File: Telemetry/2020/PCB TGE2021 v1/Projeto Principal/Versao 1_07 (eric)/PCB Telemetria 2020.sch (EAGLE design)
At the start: 58 parts, among them IC1 INA240A1DR, IC2 MCP3221A6T-E_OTVAO, IC3 AZ1117IH-3.3TRG1, IC4 ACS758LCB-050B-PFF-T, IC5 ADS1115IDGSR, IC6 ACS712-030B3, IC7 THVD2410DR, IC8 TMP235AEDCKRQ1, J1 172042-0406, J2 43045-0412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

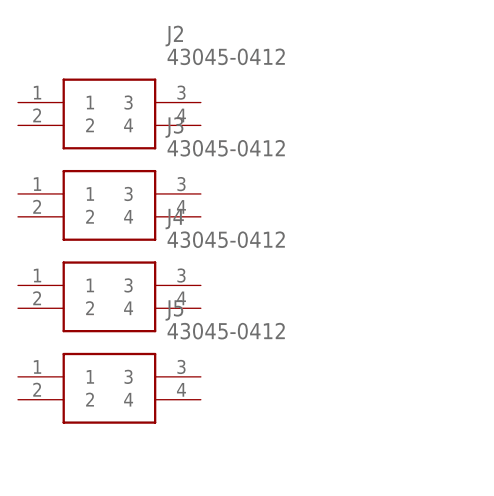
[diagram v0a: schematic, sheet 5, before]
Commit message: Final v1.07
Final version with extra connectors and temperature sensor wired properly
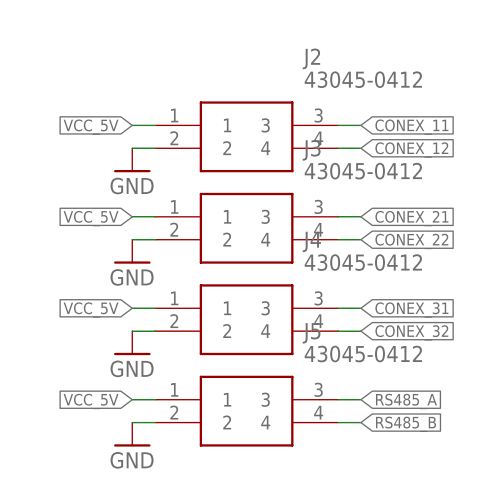
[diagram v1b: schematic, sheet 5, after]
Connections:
- removed net N$14: D2.1, IC7.B, R14.2, RJ11_1.4, RJ11_2.4
- removed net N$9: D1.1, IC7.A, R14.1, RJ11_1.2, RJ11_2.2
- new net RS485_A: D1.1, IC7.A, J5.3, R14.1, RJ11_1.2, RJ11_2.2
- new net RS485_B: D2.1, IC7.B, J5.4, R14.2, RJ11_1.4, RJ11_2.4
- net CONEX_11: now also J2.3
- net CONEX_12: now also J2.4
- net CONEX_21: now also J3.3
- net CONEX_22: now also J3.4
- net CONEX_31: now also J4.3
- net CONEX_32: now also J4.4
- net GND: now also J2.2, J3.2, J4.2, J5.2
- net VCC_5V: now also J2.1, J3.1, J4.1, J5.1
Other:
- moved on the sheet: J2, J3, J4, J5
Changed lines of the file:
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@@
 <?xml version="1.0" encoding="utf-8"?>
 <!DOCTYPE eagle SYSTEM "eagle.dtd">
-<eagle version="9.5.2">
+<eagle version="9.6.2">
 <drawing>
 <settings>
@@
 <part name="RJ11_2" library="Painel-Facilidades" deviceset="TFC44" device=""/>
 <part name="SUPPLY7" library="supply2" library_urn="urn:adsk.eagle:library:372" deviceset="GND" device=""/>
+<part name="GND20" library="supply1" library_urn="urn:adsk.eagle:library:371" deviceset="GND" device=""/>
+<part name="GND21" library="supply1" library_urn="urn:adsk.eagle:library:371" deviceset="GND" device=""/>
+<part name="GND22" library="supply1" library_urn="urn:adsk.eagle:library:371" deviceset="GND" device=""/>
+<part name="GND23" library="supply1" library_urn="urn:adsk.eagle:library:371" deviceset="GND" device=""/>
 </parts>
 <sheets>
@@
 </segment>
 </net>
-<net name="N$9" class="0">
+<net name="RS485_A" class="0">
 <segment>
 <pinref part="D1" gate="G$1" pin="1"/>
@@
 </segment>
 </net>
-<net name="N$14" class="0">
+<net name="RS485_B" class="0">
 <segment>
 <pinref part="IC7" gate="G$1" pin="B"/>
@@
 <attribute name="SHEET" x="357.505" y="5.08" size="2.54" layer="94"/>
 </instance>
-<instance part="J2" gate="G$1" x="15.24" y="246.38" smashed="yes">
-<attribute name="NAME" x="31.75" y="254" size="1.778" layer="95" align="center-left"/>
-<attribute name="VALUE" x="31.75" y="251.46" size="1.778" layer="96" align="center-left"/>
-</instance>
-<instance part="J3" gate="G$1" x="15.24" y="236.22" smashed="yes">
-<attribute name="NAME" x="31.75" y="243.84" size="1.778" layer="95" align="center-left"/>
-<attribute name="VALUE" x="31.75" y="241.3" size="1.778" layer="96" align="center-left"/>
-</instance>
-<instance part="J4" gate="G$1" x="15.24" y="226.06" smashed="yes">
-<attribute name="NAME" x="31.75" y="233.68" size="1.778" layer="95" align="center-left"/>
-<attribute name="VALUE" x="31.75" y="231.14" size="1.778" layer="96" align="center-left"/>
-</instance>
-<instance part="J5" gate="G$1" x="15.24" y="215.9" smashed="yes">
-<attribute name="NAME" x="31.75" y="223.52" size="1.778" layer="95" align="center-left"/>
-<attribute name="VALUE" x="31.75" y="220.98" size="1.778" layer="96" align="center-left"/>
+<instance part="J2" gate="G$1" x="30.48" y="243.84" smashed="yes">
+<attribute name="NAME" x="46.99" y="251.46" size="1.778" layer="95" align="center-left"/>
+<attribute name="VALUE" x="46.99" y="248.92" size="1.778" layer="96" align="center-left"/>
+</instance>
+<instance part="J3" gate="G$1" x="30.48" y="233.68" smashed="yes">
+<attribute name="NAME" x="46.99" y="241.3" size="1.778" layer="95" align="center-left"/>
+<attribute name="VALUE" x="46.99" y="238.76" size="1.778" layer="96" align="center-left"/>
+</instance>
+<instance part="J4" gate="G$1" x="30.48" y="223.52" smashed="yes">
+<attribute name="NAME" x="46.99" y="231.14" size="1.778" layer="95" align="center-left"/>
+<attribute name="VALUE" x="46.99" y="228.6" size="1.778" layer="96" align="center-left"/>
+</instance>
+<instance part="J5" gate="G$1" x="30.48" y="213.36" smashed="yes">
+<attribute name="NAME" x="46.99" y="220.98" size="1.778" layer="95" align="center-left"/>
+<attribute name="VALUE" x="46.99" y="218.44" size="1.778" layer="96" align="center-left"/>
+</instance>
+<instance part="GND20" gate="1" x="27.94" y="238.76" smashed="yes">
+<attribute name="VALUE" x="25.4" y="236.22" size="1.778" layer="96"/>
+</instance>
+<instance part="GND21" gate="1" x="27.94" y="228.6" smashed="yes">
+<attribute name="VALUE" x="25.4" y="226.06" size="1.778" layer="96"/>
+</instance>
+<instance part="GND22" gate="1" x="27.94" y="218.44" smashed="yes">
+<attribute name="VALUE" x="25.4" y="215.9" size="1.778" layer="96"/>
+</instance>
+<instance part="GND23" gate="1" x="27.94" y="208.28" smashed="yes">
+<attribute name="VALUE" x="25.4" y="205.74" size="1.778" layer="96"/>
 </instance>
 </instances>
@@
 </busses>
 <nets>
+<net name="VCC_5V" class="0">
+<segment>
+<pinref part="J2" gate="G$1" pin="1"/>
+<wire x1="30.48" y1="243.84" x2="27.94" y2="243.84" width="0.1524" layer="91"/>
+<label x="27.94" y="243.84" size="1.27" layer="95" rot="R180" xref="yes"/>
+</segment>
+<segment>
+<pinref part="J3" gate="G$1" pin="1"/>
+<wire x1="30.48" y1="233.68" x2="27.94" y2="233.68" width="0.1524" layer="91"/>
+<label x="27.94" y="233.68" size="1.27" layer="95" rot="R180" xref="yes"/>
+</segment>
+<segment>
+<pinref part="J4" gate="G$1" pin="1"/>
+<wire x1="30.48" y1="223.52" x2="27.94" y2="223.52" width="0.1524" layer="91"/>
+<label x="27.94" y="223.52" size="1.27" layer="95" rot="R180" xref="yes"/>
+</segment>
+<segment>
+<pinref part="J5" gate="G$1" pin="1"/>
+<wire x1="30.48" y1="213.36" x2="27.94" y2="213.36" width="0.1524" layer="91"/>
+<label x="27.94" y="213.36" size="1.27" layer="95" rot="R180" xref="yes"/>
+</segment>
+</net>
+<net name="GND" class="0">
+<segment>
+<pinref part="GND20" gate="1" pin="GND"/>
+<pinref part="J2" gate="G$1" pin="2"/>
+<wire x1="27.94" y1="241.3" x2="30.48" y2="241.3" width="0.1524" layer="91"/>
+</segment>
+<segment>
+<pinref part="GND21" gate="1" pin="GND"/>
+<pinref part="J3" gate="G$1" pin="2"/>
+<wire x1="27.94" y1="231.14" x2="30.48" y2="231.14" width="0.1524" layer="91"/>
+</segment>
+<segment>
+<pinref part="GND22" gate="1" pin="GND"/>
+<pinref part="J4" gate="G$1" pin="2"/>
+<wire x1="27.94" y1="220.98" x2="30.48" y2="220.98" width="0.1524" layer="91"/>
+</segment>
+<segment>
+<pinref part="GND23" gate="1" pin="GND"/>
+<pinref part="J5" gate="G$1" pin="2"/>
+<wire x1="27.94" y1="210.82" x2="30.48" y2="210.82" width="0.1524" layer="91"/>
+</segment>
+</net>
+<net name="CONEX_11" class="0">
+<segment>
+<pinref part="J2" gate="G$1" pin="3"/>
+<wire x1="50.8" y1="243.84" x2="53.34" y2="243.84" width="0.1524" layer="91"/>
+<label x="53.34" y="243.84" size="1.27" layer="95" xref="yes"/>
+</segment>
+</net>
+<net name="CONEX_12" class="0">
+<segment>
+<pinref part="J2" gate="G$1" pin="4"/>
+<wire x1="50.8" y1="241.3" x2="53.34" y2="241.3" width="0.1524" layer="91"/>
+<label x="53.34" y="241.3" size="1.27" layer="95" xref="yes"/>
+</segment>
+</net>
+<net name="CONEX_21" class="0">
+<segment>
+<pinref part="J3" gate="G$1" pin="3"/>
+<wire x1="50.8" y1="233.68" x2="53.34" y2="233.68" width="0.1524" layer="91"/>
+<label x="53.34" y="233.68" size="1.27" layer="95" xref="yes"/>
+</segment>
+</net>
+<net name="CONEX_22" class="0">
+<segment>
+<pinref part="J3" gate="G$1" pin="4"/>
+<wire x1="50.8" y1="231.14" x2="53.34" y2="231.14" width="0.1524" layer="91"/>
+<label x="53.34" y="231.14" size="1.27" layer="95" xref="yes"/>
+</segment>
+</net>
+<net name="CONEX_31" class="0">
+<segment>
+<pinref part="J4" gate="G$1" pin="3"/>
+<wire x1="50.8" y1="223.52" x2="53.34" y2="223.52" width="0.1524" layer="91"/>
+<label x="53.34" y="223.52" size="1.27" layer="95" xref="yes"/>
+</segment>
+</net>
+<net name="CONEX_32" class="0">
+<segment>
+<pinref part="J4" gate="G$1" pin="4"/>
+<wire x1="50.8" y1="220.98" x2="53.34" y2="220.98" width="0.1524" layer="91"/>
+<label x="53.34" y="220.98" size="1.27" layer="95" xref="yes"/>
+</segment>
+</net>
+<net name="RS485_A" class="0">
+<segment>
+<pinref part="J5" gate="G$1" pin="3"/>
+<wire x1="50.8" y1="213.36" x2="53.34" y2="213.36" width="0.1524" layer="91"/>
+<label x="53.34" y="213.36" size="1.27" layer="95" xref="yes"/>
+</segment>
+</net>
+<net name="RS485_B" class="0">
+<segment>
+<pinref part="J5" gate="G$1" pin="4"/>
+<wire x1="50.8" y1="210.82" x2="53.34" y2="210.82" width="0.1524" layer="91"/>
+<label x="53.34" y="210.82" size="1.27" layer="95" xref="yes"/>
+</segment>
+</net>
 </nets>
 </sheet>
